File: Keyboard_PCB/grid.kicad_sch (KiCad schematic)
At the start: 25 parts, among them SW10 7, SW11 8, SW12 9, SW13 10, SW14 11, SW15 rotary, SW3 0, SW4 1, SW5 2, SW6 3, SW7 4, SW8 5, SW9 6

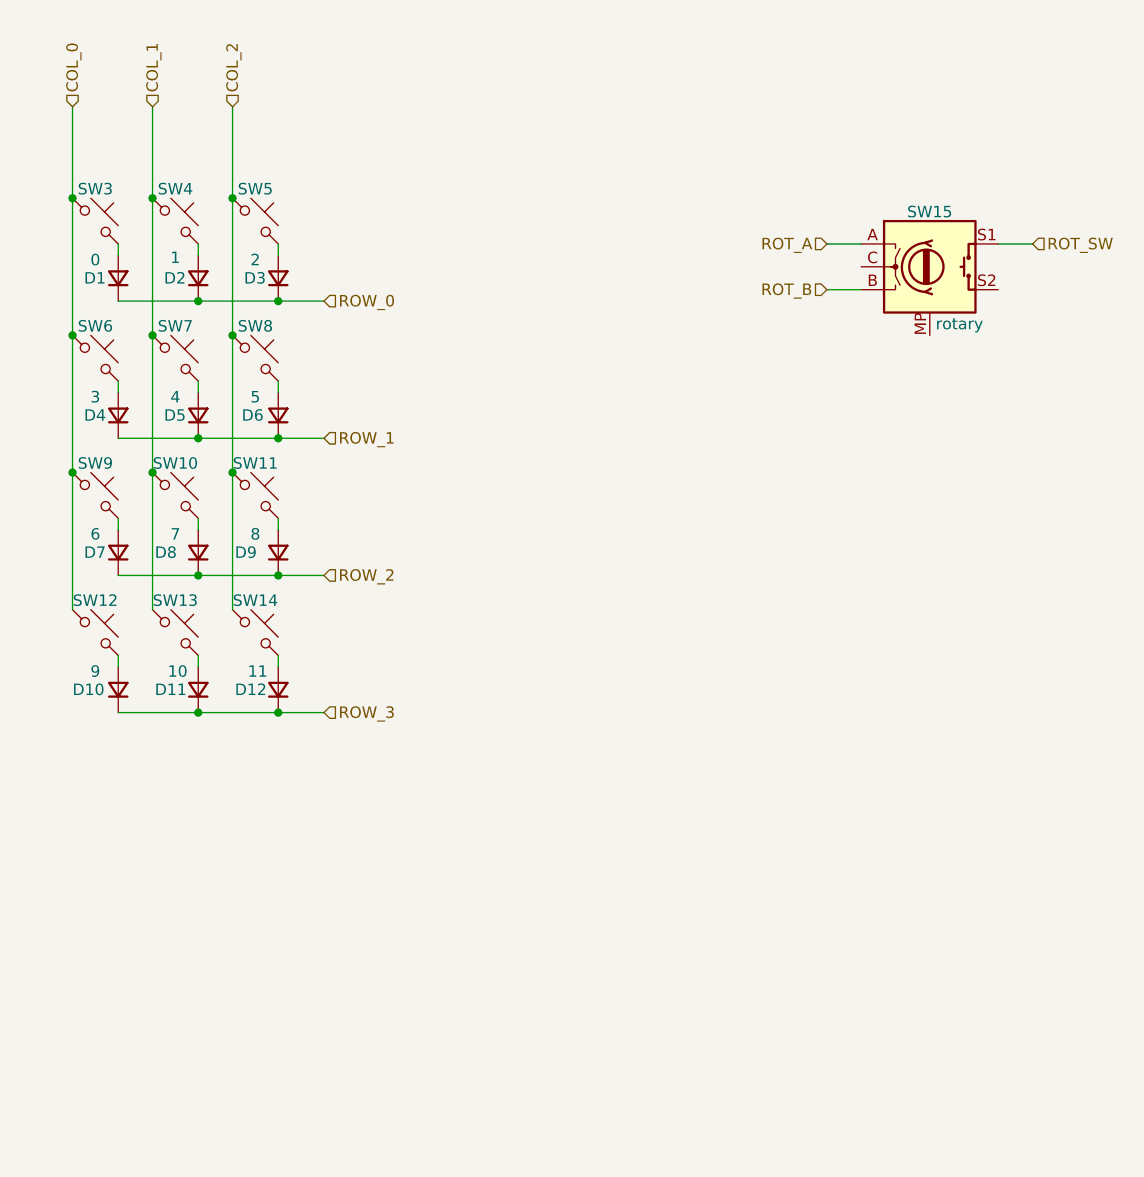
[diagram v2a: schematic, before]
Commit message: Schematic done
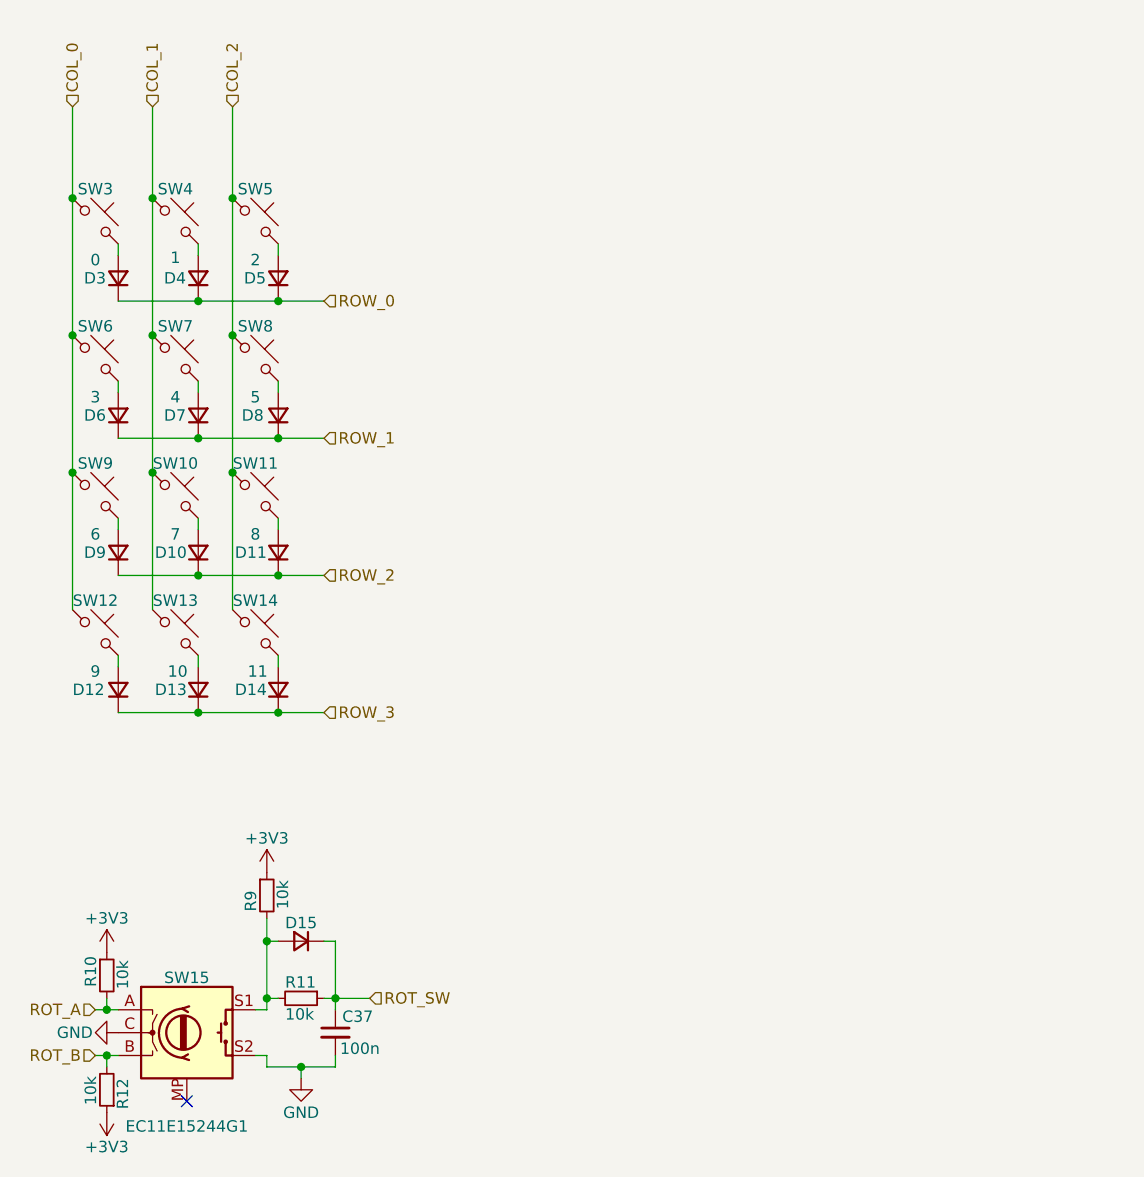
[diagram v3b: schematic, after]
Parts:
- added C37: 100n, Capacitor_SMD:C_0603_1608Metric, symbol Device:C_Small
- added D15: ~, symbol Device:D_Small
- added R10, R11, R12, R9: 10k, Resistor_SMD:R_0603_1608Metric, symbol Device:R_Small
- D10: renamed from D8; footprint Diode_SMD:D_SOD-323 -> (none)
- D11: renamed from D9; footprint Diode_SMD:D_SOD-323 -> (none)
- D12: renamed from D10; footprint Diode_SMD:D_SOD-323 -> (none)
- D13: renamed from D11; footprint Diode_SMD:D_SOD-323 -> (none)
- D14: renamed from D12; footprint Diode_SMD:D_SOD-323 -> (none)
- D3: renamed from D1; footprint Diode_SMD:D_SOD-323 -> (none)
- D4: renamed from D2; footprint Diode_SMD:D_SOD-323 -> (none)
- D5: renamed from D3; footprint Diode_SMD:D_SOD-323 -> (none)
- D6: renamed from D4; footprint Diode_SMD:D_SOD-323 -> (none)
- D7: renamed from D5; footprint Diode_SMD:D_SOD-323 -> (none)
- D8: renamed from D6; footprint Diode_SMD:D_SOD-323 -> (none)
- D9: renamed from D7; footprint Diode_SMD:D_SOD-323 -> (none)
- SW15: value rotary -> EC11E15244G1; footprint (none) -> Marijn:EC11E_rotary_MP_pads
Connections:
- net ROT_A: now also R10.2
- net ROT_B: now also R12.2
- net ROT_SW: now also C37.1, D15.1 (K), R11.1; no longer SW15.S1
- net GND: now reaches SW15.C
- net GND: now also SW15.S2, C37.2
- new net: D15.2 (A), R11.2, R9.2, SW15.S1
- new net +3V3: R10.1, R12.1, R9.1
- no-connect marks 0 -> 1
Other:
- moved on the sheet: SW15

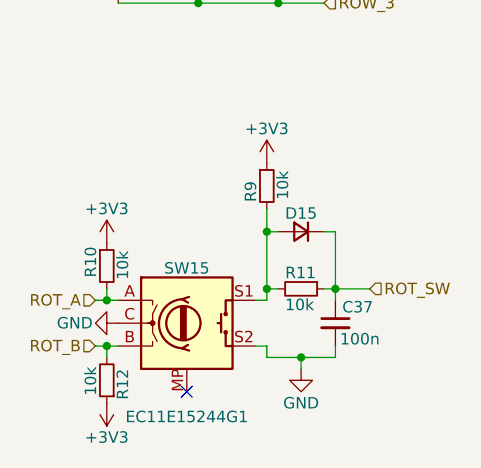
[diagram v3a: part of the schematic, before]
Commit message: eMMC routing and STM passives
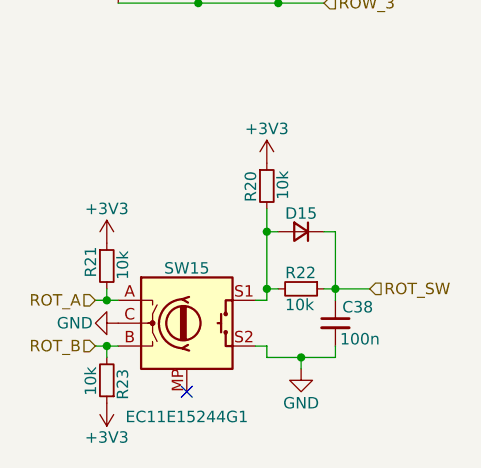
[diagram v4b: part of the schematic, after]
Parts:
- renumbered C37 to C38, R9 to R20, R10 to R21, R11 to R22, R12 to R23
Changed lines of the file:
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@@
 		(on_board yes)
 		(dnp no)
-		(property "Reference" "#PWR053"
+		(property "Reference" "#PWR066"
 			(at 82.55 139.7 0)
 			(effects
@@
 			(project ""
 				(path "/dd51e792-c76c-4d43-96de-494177f3b593/2efb7614-f68d-465d-9514-3e61f2b99fcc"
-					(reference "#PWR053")
+					(reference "#PWR066")
 					(unit 1)
 				)
@@
 		(on_board yes)
 		(dnp no)
-		(property "Reference" "R10"
+		(property "Reference" "R21"
 			(at 62.992 148.59 90)
 			(effects
@@
 			(project "Keyboard_PCB"
 				(path "/dd51e792-c76c-4d43-96de-494177f3b593/2efb7614-f68d-465d-9514-3e61f2b99fcc"
-					(reference "R10")
+					(reference "R21")
 					(unit 1)
 				)
@@
 		(on_board yes)
 		(dnp no)
-		(property "Reference" "C37"
+		(property "Reference" "C38"
 			(at 90.932 151.892 0)
 			(effects
@@
 			(project "Keyboard_PCB"
 				(path "/dd51e792-c76c-4d43-96de-494177f3b593/2efb7614-f68d-465d-9514-3e61f2b99fcc"
-					(reference "C37")
+					(reference "C38")
 					(unit 1)
 				)
@@
 		(on_board yes)
 		(dnp no)
-		(property "Reference" "R9"
+		(property "Reference" "R20"
 			(at 80.772 140.208 90)
 			(effects
@@
 			(project "Keyboard_PCB"
 				(path "/dd51e792-c76c-4d43-96de-494177f3b593/2efb7614-f68d-465d-9514-3e61f2b99fcc"
-					(reference "R9")
+					(reference "R20")
 					(unit 1)
 				)
@@
 		(on_board yes)
 		(dnp no)
-		(property "Reference" "#PWR054"
+		(property "Reference" "#PWR067"
 			(at 64.77 148.59 0)
 			(effects
@@
 			(project "Keyboard_PCB"
 				(path "/dd51e792-c76c-4d43-96de-494177f3b593/2efb7614-f68d-465d-9514-3e61f2b99fcc"
-					(reference "#PWR054")
+					(reference "#PWR067")
 					(unit 1)
 				)
@@
 		(on_board yes)
 		(dnp no)
-		(property "Reference" "#PWR057"
+		(property "Reference" "#PWR070"
 			(at 64.77 158.75 0)
 			(effects
@@
 			(project "Keyboard_PCB"
 				(path "/dd51e792-c76c-4d43-96de-494177f3b593/2efb7614-f68d-465d-9514-3e61f2b99fcc"
-					(reference "#PWR057")
+					(reference "#PWR070")
 					(unit 1)
 				)
@@
 		(on_board yes)
 		(dnp no)
-		(property "Reference" "#PWR055"
+		(property "Reference" "#PWR068"
 			(at 59.69 153.67 0)
 			(effects
@@
 			(project "Keyboard_PCB"
 				(path "/dd51e792-c76c-4d43-96de-494177f3b593/2efb7614-f68d-465d-9514-3e61f2b99fcc"
-					(reference "#PWR055")
+					(reference "#PWR068")
 					(unit 1)
 				)
@@
 		(on_board yes)
 		(dnp no)
-		(property "Reference" "R11"
+		(property "Reference" "R22"
 			(at 84.582 148.082 90)
 			(effects
@@
 			(project "Keyboard_PCB"
 				(path "/dd51e792-c76c-4d43-96de-494177f3b593/2efb7614-f68d-465d-9514-3e61f2b99fcc"
-					(reference "R11")
+					(reference "R22")
 					(unit 1)
 				)
@@
 		(on_board yes)
 		(dnp no)
-		(property "Reference" "#PWR056"
+		(property "Reference" "#PWR069"
 			(at 86.36 165.1 0)
 			(effects
@@
 			(project "Keyboard_PCB"
 				(path "/dd51e792-c76c-4d43-96de-494177f3b593/2efb7614-f68d-465d-9514-3e61f2b99fcc"
-					(reference "#PWR056")
+					(reference "#PWR069")
 					(unit 1)
 				)
@@
 		(on_board yes)
 		(dnp no)
-		(property "Reference" "R12"
+		(property "Reference" "R23"
 			(at 66.548 158.75 90)
 			(effects
@@
 			(project "Keyboard_PCB"
 				(path "/dd51e792-c76c-4d43-96de-494177f3b593/2efb7614-f68d-465d-9514-3e61f2b99fcc"
-					(reference "R12")
-					(unit 1)
-				)
+					(reference "R23")
+					(unit 1)
+				)

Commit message: Grid diode layout
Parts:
- D10, D11, D12, D13, D14, D15, D3, D4, D5, D6, D7, D8, D9: footprint (none) -> Marijn:SOD-523F
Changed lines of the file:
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@@
 			)
 		)
-		(property "Footprint" ""
+		(property "Footprint" "Marijn:SOD-523F"
 			(at 74.93 85.09 90)
 			(effects
@@
 			)
 		)
-		(property "Datasheet" "~"
+		(property "Datasheet" "https://eu.mouser.com/datasheet/2/80/CDBU0245_HF_RevB-2489203.pdf"
 			(at 74.93 85.09 90)
 			(effects
@@
 			)
 		)
-		(property "Footprint" ""
+		(property "Footprint" "Marijn:SOD-523F"
 			(at 83.82 115.57 90)
 			(effects
@@
 			)
 		)
-		(property "Datasheet" "~"
+		(property "Datasheet" "https://eu.mouser.com/datasheet/2/80/CDBU0245_HF_RevB-2489203.pdf"
 			(at 83.82 115.57 90)
 			(effects
@@
 			)
 		)
-		(property "Footprint" ""
+		(property "Footprint" "Marijn:SOD-523F"
 			(at 66.04 100.33 90)
 			(effects
@@
 			)
 		)
-		(property "Datasheet" "~"
+		(property "Datasheet" "https://eu.mouser.com/datasheet/2/80/CDBU0245_HF_RevB-2489203.pdf"
 			(at 66.04 100.33 90)
 			(effects
@@
 			)
 		)
-		(property "Footprint" ""
+		(property "Footprint" "Marijn:SOD-523F"
 			(at 74.93 100.33 90)
 			(effects
@@
 			)
 		)
-		(property "Datasheet" "~"
+		(property "Datasheet" "https://eu.mouser.com/datasheet/2/80/CDBU0245_HF_RevB-2489203.pdf"
 			(at 74.93 100.33 90)
 			(effects
@@
 			)
 		)
-		(property "Footprint" ""
+		(property "Footprint" "Marijn:SOD-523F"
 			(at 66.04 115.57 90)
 			(effects
@@
 			)
 		)
-		(property "Datasheet" "~"
+		(property "Datasheet" "https://eu.mouser.com/datasheet/2/80/CDBU0245_HF_RevB-2489203.pdf"
 			(at 66.04 115.57 90)
 			(effects
@@
 			)
 		)
-		(property "Footprint" ""
+		(property "Footprint" "Marijn:SOD-523F"
 			(at 66.04 69.85 90)
 			(effects
@@
 			)
 		)
-		(property "Datasheet" "~"
+		(property "Datasheet" "https://eu.mouser.com/datasheet/2/80/CDBU0245_HF_RevB-2489203.pdf"
 			(at 66.04 69.85 90)
 			(effects
@@
 			)
 		)
-		(property "Footprint" ""
+		(property "Footprint" "Marijn:SOD-523F"
 			(at 66.04 85.09 90)
 			(effects
@@
 			)
 		)
-		(property "Datasheet" "~"
+		(property "Datasheet" "https://eu.mouser.com/datasheet/2/80/CDBU0245_HF_RevB-2489203.pdf"
 			(at 66.04 85.09 90)
 			(effects
@@
 			)
 		)
-		(property "Footprint" ""
+		(property "Footprint" "Marijn:SOD-523F"
 			(at 74.93 69.85 90)
 			(effects
@@
 			)
 		)
-		(property "Datasheet" "~"
+		(property "Datasheet" "https://eu.mouser.com/datasheet/2/80/CDBU0245_HF_RevB-2489203.pdf"
 			(at 74.93 69.85 90)
 			(effects
@@
 			)
 		)
-		(property "Footprint" ""
+		(property "Footprint" "Marijn:SOD-523F"
 			(at 86.36 143.51 90)
 			(effects
@@
 			)
 		)
-		(property "Datasheet" "~"
+		(property "Datasheet" "https://eu.mouser.com/datasheet/2/80/CDBU0245_HF_RevB-2489203.pdf"
 			(at 86.36 143.51 90)
 			(effects
@@
 			)
 		)
-		(property "Footprint" ""
+		(property "Footprint" "Marijn:SOD-523F"
 			(at 83.82 69.85 90)
 			(effects
@@
 			)
 		)
-		(property "Datasheet" "~"
+		(property "Datasheet" "https://eu.mouser.com/datasheet/2/80/CDBU0245_HF_RevB-2489203.pdf"
 			(at 83.82 69.85 90)
 			(effects
@@
 			)
 		)
-		(property "Footprint" ""
+		(property "Footprint" "Marijn:SOD-523F"
 			(at 74.93 115.57 90)
 			(effects
@@
 			)
 		)
-		(property "Datasheet" "~"
+		(property "Datasheet" "https://eu.mouser.com/datasheet/2/80/CDBU0245_HF_RevB-2489203.pdf"
 			(at 74.93 115.57 90)
 			(effects
@@
 			)
 		)
-		(property "Footprint" ""
+		(property "Footprint" "Marijn:SOD-523F"
 			(at 83.82 100.33 90)
 			(effects
@@
 			)
 		)
-		(property "Datasheet" "~"
+		(property "Datasheet" "https://eu.mouser.com/datasheet/2/80/CDBU0245_HF_RevB-2489203.pdf"
 			(at 83.82 100.33 90)
 			(effects
@@
 			)
 		)
-		(property "Footprint" ""
+		(property "Footprint" "Marijn:SOD-523F"
 			(at 83.82 85.09 90)
 			(effects
@@
 			)
 		)
-		(property "Datasheet" "~"
+		(property "Datasheet" "https://eu.mouser.com/datasheet/2/80/CDBU0245_HF_RevB-2489203.pdf"
 			(at 83.82 85.09 90)
 			(effects

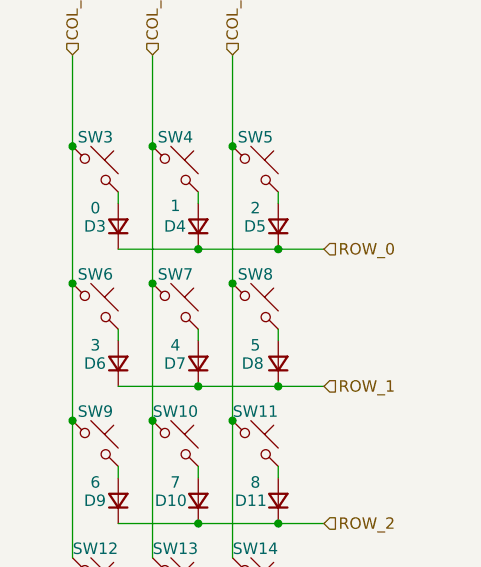
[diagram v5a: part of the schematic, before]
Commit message: Added mouser IDs to components and checked STM-eMMC connection
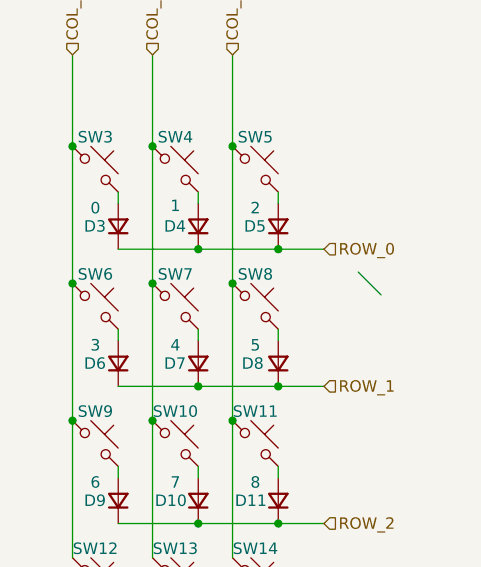
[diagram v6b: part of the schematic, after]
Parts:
- C38: Mouser 963-MCASL168SB5105MT -> (none); now left out of the parts list
- D10, D11, D12, D13, D14, D3, D4, D5, D6, D7, D8, D9: value D_Small -> ~; mouser (none) -> 750-CDBU0245
- D15: Mouser 621-1N4148W-F -> (none); mouser (none) -> 750-CDBU0245
- R20, R21, R22, R23: Mouser 603-RT0603FRE1322KL -> (none); now left out of the parts list
- SW10, SW11, SW12, SW13, SW14, SW3, SW4, SW5, SW6, SW7, SW8, SW9: now left out of the parts list
- SW15: mouser (none) -> 688-EC11E15244G1; now left out of the parts list

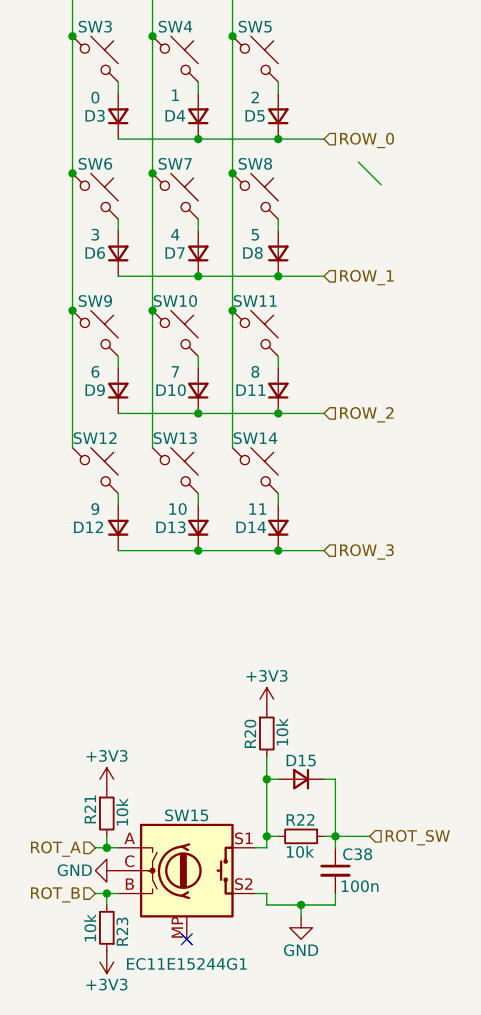
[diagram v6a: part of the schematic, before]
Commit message: Improved battery sens and added JLCPCB QR code
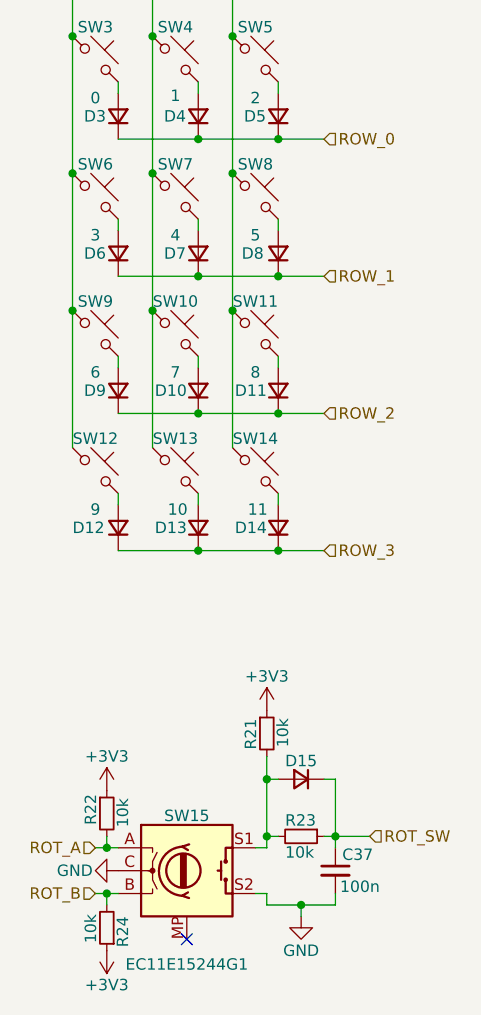
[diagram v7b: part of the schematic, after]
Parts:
- renumbered C38 to C37, R20 to R21, R21 to R22, R22 to R23, R23 to R24
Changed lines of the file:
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@@
 		(at 73.66 161.29)
 	)
-	(bus_entry
-		(at 92.71 74.93)
-		(size 2.54 2.54)
-		(stroke
-			(width 0)
-			(type default)
-		)
-	)
 	(wire
 		(pts
@@
 		(on_board yes)
 		(dnp no)
-		(property "Reference" "#PWR066"
+		(property "Reference" "#PWR068"
 			(at 82.55 139.7 0)
 			(effects
@@
 			(project ""
 				(path "/dd51e792-c76c-4d43-96de-494177f3b593/2efb7614-f68d-465d-9514-3e61f2b99fcc"
-					(reference "#PWR066")
+					(reference "#PWR068")
 					(unit 1)
 				)
@@
 		(on_board yes)
 		(dnp no)
-		(property "Reference" "R21"
+		(property "Reference" "R22"
 			(at 62.992 148.59 90)
 			(effects
@@
 			(project "Keyboard_PCB"
 				(path "/dd51e792-c76c-4d43-96de-494177f3b593/2efb7614-f68d-465d-9514-3e61f2b99fcc"
-					(reference "R21")
+					(reference "R22")
 					(unit 1)
 				)
@@
 		(on_board yes)
 		(dnp no)
-		(property "Reference" "C38"
+		(property "Reference" "C37"
 			(at 90.932 151.892 0)
 			(effects
@@
 			(project "Keyboard_PCB"
 				(path "/dd51e792-c76c-4d43-96de-494177f3b593/2efb7614-f68d-465d-9514-3e61f2b99fcc"
-					(reference "C38")
+					(reference "C37")
 					(unit 1)
 				)
@@
 		(on_board yes)
 		(dnp no)
-		(property "Reference" "R20"
+		(property "Reference" "R21"
 			(at 80.772 140.208 90)
 			(effects
@@
 			(project "Keyboard_PCB"
 				(path "/dd51e792-c76c-4d43-96de-494177f3b593/2efb7614-f68d-465d-9514-3e61f2b99fcc"
-					(reference "R20")
+					(reference "R21")
 					(unit 1)
 				)
@@
 		(on_board yes)
 		(dnp no)
-		(property "Reference" "#PWR067"
+		(property "Reference" "#PWR069"
 			(at 64.77 148.59 0)
 			(effects
@@
 			(project "Keyboard_PCB"
 				(path "/dd51e792-c76c-4d43-96de-494177f3b593/2efb7614-f68d-465d-9514-3e61f2b99fcc"
-					(reference "#PWR067")
+					(reference "#PWR069")
 					(unit 1)
 				)
@@
 		(on_board yes)
 		(dnp no)
-		(property "Reference" "#PWR070"
+		(property "Reference" "#PWR072"
 			(at 64.77 158.75 0)
 			(effects
@@
 			(project "Keyboard_PCB"
 				(path "/dd51e792-c76c-4d43-96de-494177f3b593/2efb7614-f68d-465d-9514-3e61f2b99fcc"
-					(reference "#PWR070")
+					(reference "#PWR072")
 					(unit 1)
 				)
@@
 		(on_board yes)
 		(dnp no)
-		(property "Reference" "#PWR068"
+		(property "Reference" "#PWR070"
 			(at 59.69 153.67 0)
 			(effects
@@
 			(project "Keyboard_PCB"
 				(path "/dd51e792-c76c-4d43-96de-494177f3b593/2efb7614-f68d-465d-9514-3e61f2b99fcc"
-					(reference "#PWR068")
+					(reference "#PWR070")
 					(unit 1)
 				)
@@
 		(on_board yes)
 		(dnp no)
-		(property "Reference" "R22"
+		(property "Reference" "R23"
 			(at 84.582 148.082 90)
 			(effects
@@
 			(project "Keyboard_PCB"
 				(path "/dd51e792-c76c-4d43-96de-494177f3b593/2efb7614-f68d-465d-9514-3e61f2b99fcc"
-					(reference "R22")
+					(reference "R23")
 					(unit 1)
 				)
@@
 		(on_board yes)
 		(dnp no)
-		(property "Reference" "#PWR069"
+		(property "Reference" "#PWR071"
 			(at 86.36 165.1 0)
 			(effects
@@
 			(project "Keyboard_PCB"
 				(path "/dd51e792-c76c-4d43-96de-494177f3b593/2efb7614-f68d-465d-9514-3e61f2b99fcc"
-					(reference "#PWR069")
+					(reference "#PWR071")
 					(unit 1)
 				)
@@
 		(on_board yes)
 		(dnp no)
-		(property "Reference" "R23"
+		(property "Reference" "R24"
 			(at 66.548 158.75 90)
 			(effects
@@
 			(project "Keyboard_PCB"
 				(path "/dd51e792-c76c-4d43-96de-494177f3b593/2efb7614-f68d-465d-9514-3e61f2b99fcc"
-					(reference "R23")
+					(reference "R24")
 					(unit 1)
 				)
